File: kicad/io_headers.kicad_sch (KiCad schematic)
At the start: 7 parts, among them J14 Arduino power, J15 Arduino analog, J16 Arduino digital 0-7, J17 Arduino digital 8-13, J18 Pico left (pins 1-20), J19 Pico right (pins 40-21)

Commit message: Pick JLCPCB parts for the whole BOM and add BOM/CPL generation
Adds bom/parts.csv (LCSC numbers and MPNs), scripts to apply it to the schematic and
board and to generate the JLCPCB BOM, CPL and a live stock report. Swaps the
BOOTSEL/RESET switch to a basic 5.1 mm part with a matching footprint, and replaces
out-of-stock parts (SS54, WS2812B, 10u caps, SWD header).

Co-Authored-By: Claude Sonnet 5.5 <noreply@anthropic.com>
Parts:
- J14, J16: LCSC (none) -> C124416; MPN 1x8 2.54 mm female header -> B-2200S08P-A120
- J15: LCSC (none) -> C124415; MPN 1x6 2.54 mm female header -> B-2200S06P-A120
- J17: LCSC (none) -> C124423; MPN 1x10 2.54 mm female header -> B-2200S10P-B120
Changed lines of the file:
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@@
     (stroke (width 0) (type default))
   )
-  (wire (pts (xy 381.0 68.58) (xy 375.92 68.58))
+  (wire (pts (xy 381 68.58) (xy 375.92 68.58))
     (stroke (width 0) (type default))
   )
@@
     (stroke (width 0) (type default))
   )
-  (wire (pts (xy 58.42 254.0) (xy 50.8 254.0))
+  (wire (pts (xy 58.42 254) (xy 50.8 254))
     (stroke (width 0) (type default))
   )
@@
     (stroke (width 0) (type default))
   )
-  (wire (pts (xy 147.32 254.0) (xy 139.7 254.0))
+  (wire (pts (xy 147.32 254) (xy 139.7 254))
     (stroke (width 0) (type default))
   )
@@
   )
   (text "Analog header 1x6: A0-A3 = GPIO40-43 (ADC0-3), A4 = SDA (GPIO20), A5 = SCL (GPIO21)."
-    (at 127.0 58.42 0)
+    (at 127 58.42 0)
     (effects (font (size 1.8 1.8)) (justify left))
   )
@@
     )
   )
-  (global_label "GPIO7" (shape bidirectional) (at 50.8 254.0 180)
-    (effects (font (size 1.27 1.27)) (justify right))
-    (property "Intersheetrefs" "${INTERSHEET_REFS}" (id 0) (at 50.8 254.0 0)
+  (global_label "GPIO7" (shape bidirectional) (at 50.8 254 180)
+    (effects (font (size 1.27 1.27)) (justify right))
+    (property "Intersheetrefs" "${INTERSHEET_REFS}" (id 0) (at 50.8 254 0)
       (effects (font (size 1.27 1.27)) hide)
     )
@@
     )
   )
-  (global_label "GPIO26" (shape bidirectional) (at 139.7 254.0 180)
-    (effects (font (size 1.27 1.27)) (justify right))
-    (property "Intersheetrefs" "${INTERSHEET_REFS}" (id 0) (at 139.7 254.0 0)
+  (global_label "GPIO26" (shape bidirectional) (at 139.7 254 180)
+    (effects (font (size 1.27 1.27)) (justify right))
+    (property "Intersheetrefs" "${INTERSHEET_REFS}" (id 0) (at 139.7 254 0)
       (effects (font (size 1.27 1.27)) hide)
     )
@@
       (effects (font (size 1.27 1.27)) hide)
     )
-    (property "MPN" "1x8 2.54 mm female header" (id 4) (at 63.5 76.2 0)
+    (property "MPN" "B-2200S08P-A120" (id 4) (at 63.5 76.2 0)
+      (effects (font (size 1.27 1.27)) hide)
+    )
+    (property "LCSC" "C124416" (id 5) (at 63.5 66.04 0)
       (effects (font (size 1.27 1.27)) hide)
     )
@@
       (effects (font (size 1.27 1.27)) hide)
     )
-    (property "MPN" "1x6 2.54 mm female header" (id 4) (at 152.4 76.2 0)
+    (property "MPN" "B-2200S06P-A120" (id 4) (at 152.4 76.2 0)
+      (effects (font (size 1.27 1.27)) hide)
+    )
+    (property "LCSC" "C124415" (id 5) (at 152.4 68.58 0)
       (effects (font (size 1.27 1.27)) hide)
     )
@@
       (effects (font (size 1.27 1.27)) hide)
     )
-    (property "MPN" "1x8 2.54 mm female header" (id 4) (at 241.3 76.2 0)
+    (property "MPN" "B-2200S08P-A120" (id 4) (at 241.3 76.2 0)
+      (effects (font (size 1.27 1.27)) hide)
+    )
+    (property "LCSC" "C124416" (id 5) (at 241.3 66.04 0)
       (effects (font (size 1.27 1.27)) hide)
     )
@@
       (effects (font (size 1.27 1.27)) hide)
     )
-    (property "MPN" "1x10 2.54 mm female header" (id 4) (at 330.20000000000005 76.2 0)
+    (property "MPN" "B-2200S10P-B120" (id 4) (at 330.20000000000005 76.2 0)
+      (effects (font (size 1.27 1.27)) hide)
+    )
+    (property "LCSC" "C124423" (id 5) (at 330.2 63.5 0)
       (effects (font (size 1.27 1.27)) hide)
     )
@@
     )
   )
-  (symbol (lib_id "Connector_Generic:Conn_01x20") (at 63.5 254.0 0) (unit 1)
+  (symbol (lib_id "Connector_Generic:Conn_01x20") (at 63.5 254 0) (unit 1)
     (in_bom yes) (on_board yes) (dnp no)
     (property "Reference" "J18" (id 0) (at 63.5 228.6 0)
@@
       (effects (font (size 1.27 1.27)))
     )
-    (property "Footprint" "Connector_PinSocket_2.54mm:PinSocket_1x20_P2.54mm_Vertical" (id 2) (at 63.5 254.0 0)
-      (effects (font (size 1.27 1.27)) hide)
-    )
-    (property "Datasheet" "" (id 3) (at 63.5 254.0 0)
-      (effects (font (size 1.27 1.27)) hide)
-    )
-    (property "LCSC" "C124410" (id 4) (at 63.5 254.0 0)
-      (effects (font (size 1.27 1.27)) hide)
-    )
-    (property "MPN" "B-2200S20P-A120 (1x20 female)" (id 5) (at 63.5 254.0 0)
+    (property "Footprint" "Connector_PinSocket_2.54mm:PinSocket_1x20_P2.54mm_Vertical" (id 2) (at 63.5 254 0)
+      (effects (font (size 1.27 1.27)) hide)
+    )
+    (property "Datasheet" "" (id 3) (at 63.5 254 0)
+      (effects (font (size 1.27 1.27)) hide)
+    )
+    (property "LCSC" "C124410" (id 4) (at 63.5 254 0)
+      (effects (font (size 1.27 1.27)) hide)
+    )
+    (property "MPN" "B-2200S20P-A120 (1x20 female)" (id 5) (at 63.5 254 0)
       (effects (font (size 1.27 1.27)) hide)
     )
@@
     )
   )
-  (symbol (lib_id "Connector_Generic:Conn_01x20") (at 152.4 254.0 0) (unit 1)
+  (symbol (lib_id "Connector_Generic:Conn_01x20") (at 152.4 254 0) (unit 1)
     (in_bom yes) (on_board yes) (dnp no)
     (property "Reference" "J19" (id 0) (at 152.4 228.6 0)
@@
       (effects (font (size 1.27 1.27)))
     )
-    (property "Footprint" "Connector_PinSocket_2.54mm:PinSocket_1x20_P2.54mm_Vertical" (id 2) (at 152.4 254.0 0)
-      (effects (font (size 1.27 1.27)) hide)
-    )
-    (property "Datasheet" "" (id 3) (at 152.4 254.0 0)
-      (effects (font (size 1.27 1.27)) hide)
-    )
-    (property "LCSC" "C124410" (id 4) (at 152.4 254.0 0)
-      (effects (font (size 1.27 1.27)) hide)
-    )
-    (property "MPN" "B-2200S20P-A120 (1x20 female)" (id 5) (at 152.4 254.0 0)
-      (effects (font (size 1.27 1.27)) hide)
-    )
+    (property "Footprint" "Connector_PinSocket_2.54mm:PinSocket_1x20_P2.54mm_Vertical" (id 2) (at 152.4 254 0)
+      (effects (font (size 1.27 1.27)) hide)
+    )
+    (property "Datasheet" "" (id 3) (at 152.4 254 0)
+      (effects (font (size 1.27 1.27)) hide)
+    )
+    (property "LCSC" "C124410" (id 4) (at 152.4 254 0)
+      (effects (font (size 1.27 1.27)) hide)
+    )
+    (property "MPN" "B-2200S20P-A120 (1x20 female)" (id 5) (at 152.4 254 0)
+      (effects (font (size 1.27 1.27)) hide)
+    )

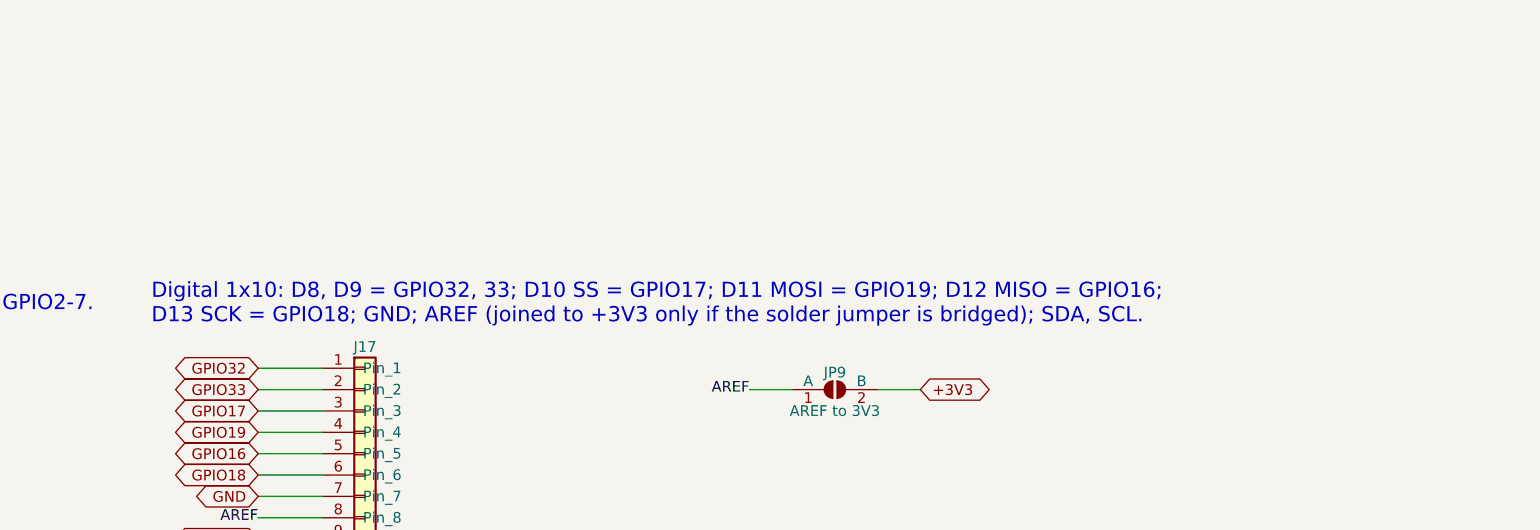
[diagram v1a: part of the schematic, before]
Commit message: Rework board layout, swap SWD header to through-hole, add Qwiic port
- SWD (J10) is now a 1x3 2.54 mm through-hole pin header footprint
  (SWCLK, GND, SWDIO) instead of the JST SH connector; removed from the
  JLCPCB BOM.
- Add J20 Qwiic connector (XY-SM04B-SRSS-TB) on the I2C bus: GND, +3V3,
  GPIO20 (SDA), GPIO21 (SCL), mounting tabs to GND.
- Placement/routing progress and the helper scripts used for it.

DRC still reports open items (unrouted RUN/GPIO24/GPIO29/QSPI_SD0 nets,
R108/GPIO23 and NT1/GPIO20 shorts, J12 edge clearance, silkscreen
overlaps); to be fixed in follow-up commits.

Co-Authored-By: Claude Sonnet 5.5 <noreply@anthropic.com>
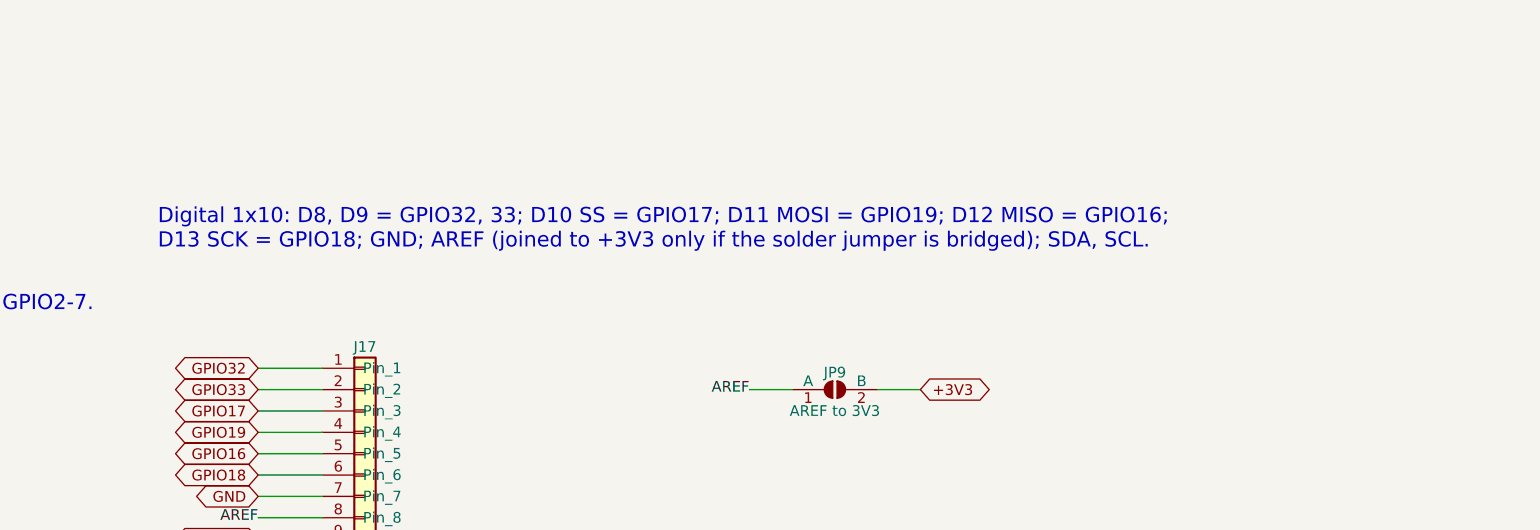
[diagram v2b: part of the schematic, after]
